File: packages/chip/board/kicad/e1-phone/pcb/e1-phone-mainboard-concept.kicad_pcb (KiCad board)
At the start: 10 copper layers, 64 x 132 mm, 87 parts

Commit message: chip(e1-phone): re-render exploded animation with corrected framing + lighting + EGL chunking
Visual self-review of the previous render exposed three defects that this commit closes:

- Camera was at radius 220 mm with 35deg yfov; phone is ~155 mm tall with parts that fly ~150 mm outward at peak explode, so the camera was effectively inside the explosion bubble. Bumped radius to 500 mm and narrowed yfov to 28deg; tilt to 15deg.
- Lights were camera-anchored, so the back of the orange shell went muddy during the 360deg orbit. Switched to world-anchored 3-point lighting.
- pyrender EGL leaked GPU memory and consistently died around frame ~150. Recreating OffscreenRenderer every 30 frames keeps the full 360-frame render stable.

Re-render output (all confirmed by reading 4 keyframes):
- e1-phone-exploded.mp4: 1920x1080, 30 fps, 12 s, h264/yuv420p, 897 KB
- e1-phone-exploded.glb: 98 nodes, 97 meshes, 3 clips (explode/reassemble/turntable), 183 KB
- e1-phone-exploded-frames/: 360 sequential frames + 24 keyframes at 0.5 s

Also restores the chip e1-phone artifacts (mechanical, board, supplier-pinouts, generator scripts) that an out-of-band git reset to origin/develop wiped between my previous commits ae3f83e9e7 / bd0a350198 and the current HEAD.

Co-Authored-By: Claude Opus 4.7 (1M context) <noreply@anthropic.com>
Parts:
- J_CAM0_CAM1: value rear_and_front_mipi_csi_cameras -> rear_and_front_mipi_csi_camera_fpc_connector_escape
- J_DISPLAY_TOUCH: value 5p5_in_fhd_mipi_display_touch -> 5p5_in_fhd_mipi_display_touch_fpc_connector_escape
- U_AUDIO_SPK_MIC: value speakers_microphones_audio_codec_haptics -> bottom_left_audio_codec_speaker_microphone_haptic_co
- moved U_AUDIO_SPK_MIC 19.6 mm to (14.0, 124.0)
- moved SW_POWER_VOL 14.0 mm to (24.0, 27.5)
- moved U_PMIC_CHARGER 13.7 mm to (24.5, 22.0)
- moved J_BATTERY 13.0 mm to (37.0, 28.0)
- moved J_DISPLAY_TOUCH 10.7 mm to (53.5, 7.00)
- moved U_CELL 7.52 mm to (10.0, 10.0)
- moved J_CAM0_CAM1 3.50 mm to (53.5, 18.5)
- moved U_WIFI_BT 2.50 mm to (10.0, 23.0)
- moved J_USB_C 2.00 mm to (34.0, 129.0)
- moved U_SOC_LPDDR_UFS 2.00 mm to (30.5, 10.0)
- moved RN_PMIC_CTL 1.20 mm to (38.0, 27.8)
- moved C_AON 1.00 mm to (18.0, 27.8)
- moved J_TOP_BOTTOM_FLEX_TOP 1.00 mm to (54.0, 27.5)
- moved RC_1 1.00 mm to (3.00, 27.8)
- moved RC_2 1.00 mm to (8.00, 27.8)
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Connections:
- J_TOP_BOTTOM_FLEX_BOTTOM pad 1: USB_DP -> GND
- J_TOP_BOTTOM_FLEX_BOTTOM pad 10: VDD_AUDIO_3V3 -> VBUS
- J_TOP_BOTTOM_FLEX_BOTTOM pad 11: VDD_AMP_3V3 -> GND
- J_TOP_BOTTOM_FLEX_BOTTOM pad 12: I2S_BCLK -> SYS
- J_TOP_BOTTOM_FLEX_BOTTOM pad 13: I2S_LRCLK -> GND
- J_TOP_BOTTOM_FLEX_BOTTOM pad 14: I2S_DOUT -> SYS
- J_TOP_BOTTOM_FLEX_BOTTOM pad 15: I2S_DIN -> AON_1V8
- J_TOP_BOTTOM_FLEX_BOTTOM pad 16: PDM_CLK -> GND
- J_TOP_BOTTOM_FLEX_BOTTOM pad 17: PDM_DAT -> IO_1V8
- J_TOP_BOTTOM_FLEX_BOTTOM pad 18: AUDIO_I2C_SCL -> GND
- J_TOP_BOTTOM_FLEX_BOTTOM pad 19: AUDIO_I2C_SDA -> VDD_AUDIO_3V3
- J_TOP_BOTTOM_FLEX_BOTTOM pad 2: USB_DN -> USB_DP
- J_TOP_BOTTOM_FLEX_BOTTOM pad 20: CODEC_INT -> VDD_AMP_3V3
- J_TOP_BOTTOM_FLEX_BOTTOM pad 21: AMP_INT -> GND
- J_TOP_BOTTOM_FLEX_BOTTOM pad 22: HAPTIC_OUT -> VBAT
- J_TOP_BOTTOM_FLEX_BOTTOM pad 23: VBAT -> GND
- J_TOP_BOTTOM_FLEX_BOTTOM pad 26: GND -> I2S_BCLK
- J_TOP_BOTTOM_FLEX_BOTTOM pad 28: GND -> I2S_LRCLK
- J_TOP_BOTTOM_FLEX_BOTTOM pad 29: GND -> I2S_DOUT
- J_TOP_BOTTOM_FLEX_BOTTOM pad 3: USB_CC1 -> USB_DN
- J_TOP_BOTTOM_FLEX_BOTTOM pad 30: GND -> I2S_DIN
- J_TOP_BOTTOM_FLEX_BOTTOM pad 32: GND -> PDM_CLK
- J_TOP_BOTTOM_FLEX_BOTTOM pad 34: GND -> PDM_DAT
- J_TOP_BOTTOM_FLEX_BOTTOM pad 35: GND -> AUDIO_I2C_SCL
- J_TOP_BOTTOM_FLEX_BOTTOM pad 36: GND -> AUDIO_I2C_SDA
- J_TOP_BOTTOM_FLEX_BOTTOM pad 37: GND -> CODEC_INT
- J_TOP_BOTTOM_FLEX_BOTTOM pad 38: GND -> AMP_INT
- J_TOP_BOTTOM_FLEX_BOTTOM pad 39: GND -> HAPTIC_OUT
- J_TOP_BOTTOM_FLEX_BOTTOM pad 4: USB_CC2 -> GND
- J_TOP_BOTTOM_FLEX_BOTTOM pad 41: GND -> (no net)
- J_TOP_BOTTOM_FLEX_BOTTOM pad 42: GND -> (no net)
- J_TOP_BOTTOM_FLEX_BOTTOM pad 43: GND -> (no net)
- J_TOP_BOTTOM_FLEX_BOTTOM pad 44: GND -> (no net)
- J_TOP_BOTTOM_FLEX_BOTTOM pad 45: GND -> (no net)
- J_TOP_BOTTOM_FLEX_BOTTOM pad 46: GND -> (no net)
- J_TOP_BOTTOM_FLEX_BOTTOM pad 5: VBUS -> SHIELD_GND
- J_TOP_BOTTOM_FLEX_BOTTOM pad 6: SHIELD_GND -> USB_CC1
- J_TOP_BOTTOM_FLEX_BOTTOM pad 7: SYS -> USB_CC2
- J_TOP_BOTTOM_FLEX_BOTTOM pad 8: AON_1V8 -> VBUS
- J_TOP_BOTTOM_FLEX_BOTTOM pad 9: IO_1V8 -> GND
- J_TOP_BOTTOM_FLEX_TOP pad 1: USB_DP -> GND
- J_TOP_BOTTOM_FLEX_TOP pad 10: VDD_AUDIO_3V3 -> VBUS
- J_TOP_BOTTOM_FLEX_TOP pad 11: VDD_AMP_3V3 -> GND
- J_TOP_BOTTOM_FLEX_TOP pad 12: I2S_BCLK -> SYS
- J_TOP_BOTTOM_FLEX_TOP pad 13: I2S_LRCLK -> GND
- J_TOP_BOTTOM_FLEX_TOP pad 14: I2S_DOUT -> SYS
- J_TOP_BOTTOM_FLEX_TOP pad 15: I2S_DIN -> AON_1V8
- J_TOP_BOTTOM_FLEX_TOP pad 16: PDM_CLK -> GND
- J_TOP_BOTTOM_FLEX_TOP pad 17: PDM_DAT -> IO_1V8
- J_TOP_BOTTOM_FLEX_TOP pad 18: AUDIO_I2C_SCL -> GND
- J_TOP_BOTTOM_FLEX_TOP pad 19: AUDIO_I2C_SDA -> VDD_AUDIO_3V3
- J_TOP_BOTTOM_FLEX_TOP pad 2: USB_DN -> USB_DP
- J_TOP_BOTTOM_FLEX_TOP pad 20: CODEC_INT -> VDD_AMP_3V3
- J_TOP_BOTTOM_FLEX_TOP pad 21: AMP_INT -> GND
- J_TOP_BOTTOM_FLEX_TOP pad 22: HAPTIC_OUT -> VBAT
- J_TOP_BOTTOM_FLEX_TOP pad 23: VBAT -> GND
- J_TOP_BOTTOM_FLEX_TOP pad 26: GND -> I2S_BCLK
- J_TOP_BOTTOM_FLEX_TOP pad 28: GND -> I2S_LRCLK
- J_TOP_BOTTOM_FLEX_TOP pad 29: GND -> I2S_DOUT
- J_TOP_BOTTOM_FLEX_TOP pad 3: USB_CC1 -> USB_DN
- J_TOP_BOTTOM_FLEX_TOP pad 30: GND -> I2S_DIN
- J_TOP_BOTTOM_FLEX_TOP pad 32: GND -> PDM_CLK
- J_TOP_BOTTOM_FLEX_TOP pad 34: GND -> PDM_DAT
- J_TOP_BOTTOM_FLEX_TOP pad 35: GND -> AUDIO_I2C_SCL
- J_TOP_BOTTOM_FLEX_TOP pad 36: GND -> AUDIO_I2C_SDA
- J_TOP_BOTTOM_FLEX_TOP pad 37: GND -> CODEC_INT
- J_TOP_BOTTOM_FLEX_TOP pad 38: GND -> AMP_INT
- J_TOP_BOTTOM_FLEX_TOP pad 39: GND -> HAPTIC_OUT
- J_TOP_BOTTOM_FLEX_TOP pad 4: USB_CC2 -> GND
- J_TOP_BOTTOM_FLEX_TOP pad 41: GND -> (no net)
- J_TOP_BOTTOM_FLEX_TOP pad 42: GND -> (no net)
- J_TOP_BOTTOM_FLEX_TOP pad 43: GND -> (no net)
- J_TOP_BOTTOM_FLEX_TOP pad 44: GND -> (no net)
- J_TOP_BOTTOM_FLEX_TOP pad 45: GND -> (no net)
- J_TOP_BOTTOM_FLEX_TOP pad 46: GND -> (no net)
- J_TOP_BOTTOM_FLEX_TOP pad 5: VBUS -> SHIELD_GND
- J_TOP_BOTTOM_FLEX_TOP pad 6: SHIELD_GND -> USB_CC1
- J_TOP_BOTTOM_FLEX_TOP pad 7: SYS -> USB_CC2
- J_TOP_BOTTOM_FLEX_TOP pad 8: AON_1V8 -> VBUS
- J_TOP_BOTTOM_FLEX_TOP pad 9: IO_1V8 -> GND
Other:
- net class E1Phone_AUDIO_ANALOG_HAPTIC added: clearance 0.160, trace_width 0.160, via_dia 0.300, via_drill 0.150
- net class E1Phone_DEBUG_BOOT added: clearance 0.100, trace_width 0.100, via_dia 0.250, via_drill 0.100
- net class E1Phone_DISPLAY_CAMERA_CONTROL added: clearance 0.100, trace_width 0.100, via_dia 0.250, via_drill 0.100
- net class E1Phone_POWER_SENSE_CONTROL added: clearance 0.100, trace_width 0.100, via_dia 0.250, via_drill 0.100
- net class E1Phone_USB_CC_PD_CONTROL added: clearance 0.100, trace_width 0.100, via_dia 0.250, via_drill 0.100
- net class E1Phone_WIRELESS_CONTROL_BT_UART added: clearance 0.100, trace_width 0.100, via_dia 0.250, via_drill 0.100

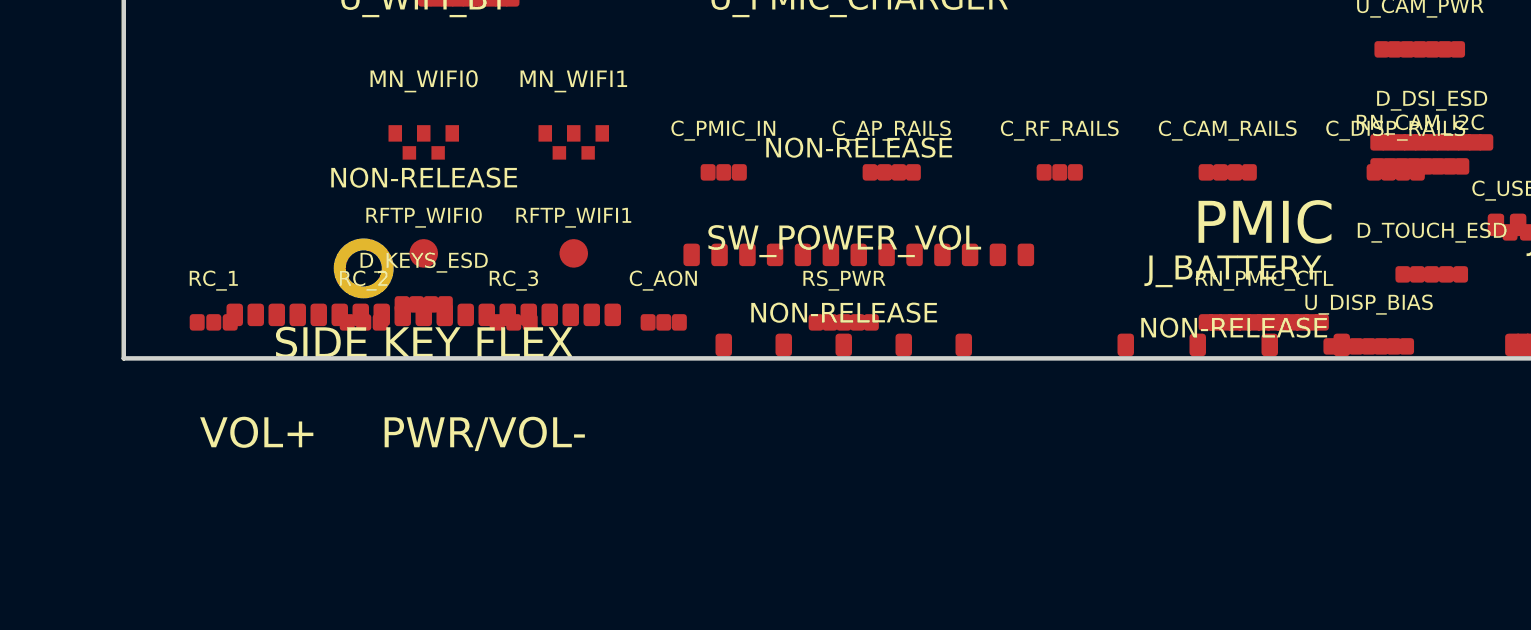
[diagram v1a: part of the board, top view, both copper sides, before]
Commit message: chore: snapshot in-flight working tree (chip/robot/android/os/riscv64/cloud)
WIP snapshot to avoid losing accumulated work across the chip board design,
robot RL + assets, android packaging, riscv64 port, and OS live-build dirs.
Generated artifacts and embedded vendor repos are excluded via .gitignore.

Co-Authored-By: Claude Opus 4.7 (1M context) <noreply@anthropic.com>
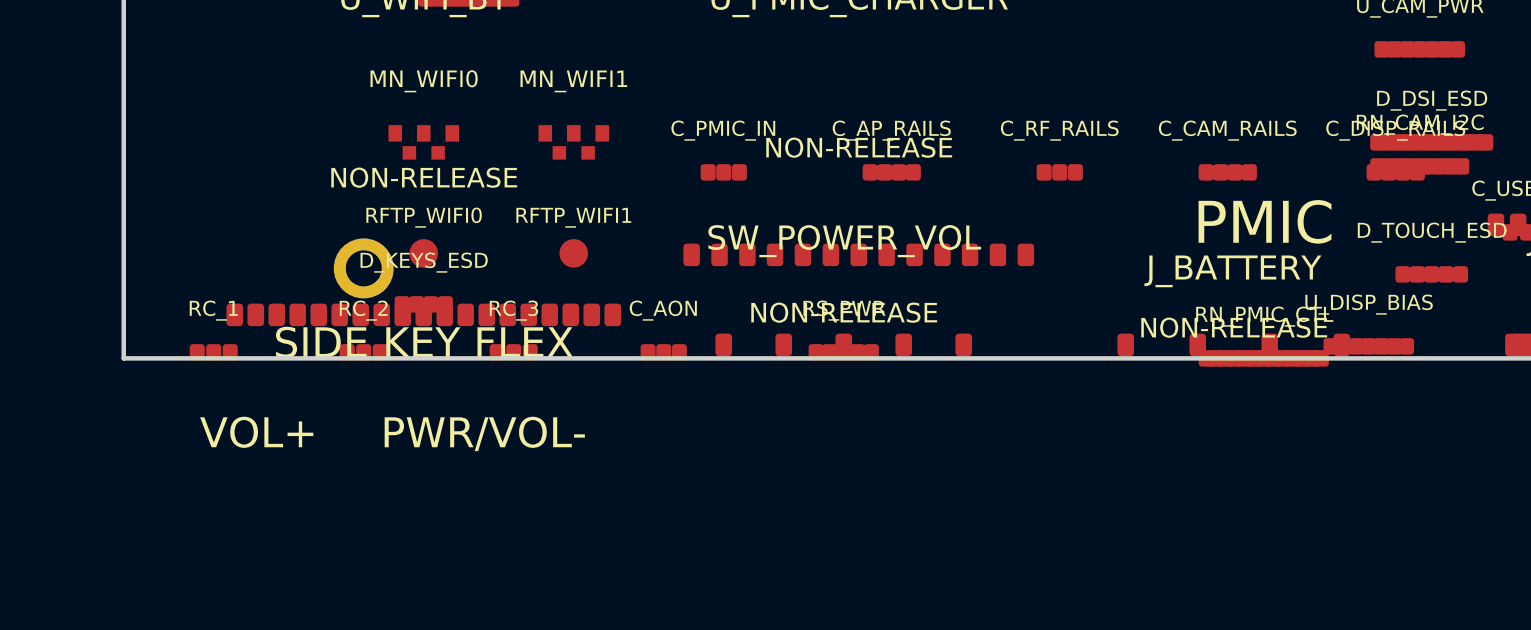
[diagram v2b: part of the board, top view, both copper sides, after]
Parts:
- moved RN_PMIC_CTL 1.20 mm to (38.0, 29.0)
- moved C_AON 1.00 mm to (18.0, 28.8)
- moved RC_1 1.00 mm to (3.00, 28.8)
- moved RC_2 1.00 mm to (8.00, 28.8)
- moved RC_3 1.00 mm to (13.0, 28.8)
- moved RS_PWR 1.00 mm to (24.0, 28.8)
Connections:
- J_TOP_BOTTOM_FLEX_BOTTOM pad 1: GND -> USB_DP
- J_TOP_BOTTOM_FLEX_BOTTOM pad 10: VBUS -> VDD_AUDIO_3V3
- J_TOP_BOTTOM_FLEX_BOTTOM pad 11: GND -> VDD_AMP_3V3
- J_TOP_BOTTOM_FLEX_BOTTOM pad 12: SYS -> I2S_BCLK
- J_TOP_BOTTOM_FLEX_BOTTOM pad 13: GND -> I2S_LRCLK
- J_TOP_BOTTOM_FLEX_BOTTOM pad 14: SYS -> I2S_DOUT
- J_TOP_BOTTOM_FLEX_BOTTOM pad 15: AON_1V8 -> I2S_DIN
- J_TOP_BOTTOM_FLEX_BOTTOM pad 16: GND -> PDM_CLK
- J_TOP_BOTTOM_FLEX_BOTTOM pad 17: IO_1V8 -> PDM_DAT
- J_TOP_BOTTOM_FLEX_BOTTOM pad 18: GND -> AUDIO_I2C_SCL
- J_TOP_BOTTOM_FLEX_BOTTOM pad 19: VDD_AUDIO_3V3 -> AUDIO_I2C_SDA
- J_TOP_BOTTOM_FLEX_BOTTOM pad 2: USB_DP -> USB_DN
- J_TOP_BOTTOM_FLEX_BOTTOM pad 20: VDD_AMP_3V3 -> CODEC_INT
- J_TOP_BOTTOM_FLEX_BOTTOM pad 21: GND -> AMP_INT
- J_TOP_BOTTOM_FLEX_BOTTOM pad 22: VBAT -> HAPTIC_OUT
- J_TOP_BOTTOM_FLEX_BOTTOM pad 23: GND -> VBAT
- J_TOP_BOTTOM_FLEX_BOTTOM pad 26: I2S_BCLK -> GND
- J_TOP_BOTTOM_FLEX_BOTTOM pad 28: I2S_LRCLK -> GND
- J_TOP_BOTTOM_FLEX_BOTTOM pad 29: I2S_DOUT -> GND
- J_TOP_BOTTOM_FLEX_BOTTOM pad 3: USB_DN -> USB_CC1
- J_TOP_BOTTOM_FLEX_BOTTOM pad 30: I2S_DIN -> GND
- J_TOP_BOTTOM_FLEX_BOTTOM pad 32: PDM_CLK -> GND
- J_TOP_BOTTOM_FLEX_BOTTOM pad 34: PDM_DAT -> GND
- J_TOP_BOTTOM_FLEX_BOTTOM pad 35: AUDIO_I2C_SCL -> GND
- J_TOP_BOTTOM_FLEX_BOTTOM pad 36: AUDIO_I2C_SDA -> GND
- J_TOP_BOTTOM_FLEX_BOTTOM pad 37: CODEC_INT -> GND
- J_TOP_BOTTOM_FLEX_BOTTOM pad 38: AMP_INT -> GND
- J_TOP_BOTTOM_FLEX_BOTTOM pad 39: HAPTIC_OUT -> GND
- J_TOP_BOTTOM_FLEX_BOTTOM pad 4: GND -> USB_CC2
- J_TOP_BOTTOM_FLEX_BOTTOM pad 41: (no net) -> GND
- J_TOP_BOTTOM_FLEX_BOTTOM pad 42: (no net) -> GND
- J_TOP_BOTTOM_FLEX_BOTTOM pad 43: (no net) -> GND
- J_TOP_BOTTOM_FLEX_BOTTOM pad 44: (no net) -> GND
- J_TOP_BOTTOM_FLEX_BOTTOM pad 45: (no net) -> GND
- J_TOP_BOTTOM_FLEX_BOTTOM pad 46: (no net) -> GND
- J_TOP_BOTTOM_FLEX_BOTTOM pad 5: SHIELD_GND -> VBUS
- J_TOP_BOTTOM_FLEX_BOTTOM pad 6: USB_CC1 -> SHIELD_GND
- J_TOP_BOTTOM_FLEX_BOTTOM pad 7: USB_CC2 -> SYS
- J_TOP_BOTTOM_FLEX_BOTTOM pad 8: VBUS -> AON_1V8
- J_TOP_BOTTOM_FLEX_BOTTOM pad 9: GND -> IO_1V8
- J_TOP_BOTTOM_FLEX_TOP pad 1: GND -> USB_DP
- J_TOP_BOTTOM_FLEX_TOP pad 10: VBUS -> VDD_AUDIO_3V3
- J_TOP_BOTTOM_FLEX_TOP pad 11: GND -> VDD_AMP_3V3
- J_TOP_BOTTOM_FLEX_TOP pad 12: SYS -> I2S_BCLK
- J_TOP_BOTTOM_FLEX_TOP pad 13: GND -> I2S_LRCLK
- J_TOP_BOTTOM_FLEX_TOP pad 14: SYS -> I2S_DOUT
- J_TOP_BOTTOM_FLEX_TOP pad 15: AON_1V8 -> I2S_DIN
- J_TOP_BOTTOM_FLEX_TOP pad 16: GND -> PDM_CLK
- J_TOP_BOTTOM_FLEX_TOP pad 17: IO_1V8 -> PDM_DAT
- J_TOP_BOTTOM_FLEX_TOP pad 18: GND -> AUDIO_I2C_SCL
- J_TOP_BOTTOM_FLEX_TOP pad 19: VDD_AUDIO_3V3 -> AUDIO_I2C_SDA
- J_TOP_BOTTOM_FLEX_TOP pad 2: USB_DP -> USB_DN
- J_TOP_BOTTOM_FLEX_TOP pad 20: VDD_AMP_3V3 -> CODEC_INT
- J_TOP_BOTTOM_FLEX_TOP pad 21: GND -> AMP_INT
- J_TOP_BOTTOM_FLEX_TOP pad 22: VBAT -> HAPTIC_OUT
- J_TOP_BOTTOM_FLEX_TOP pad 23: GND -> VBAT
- J_TOP_BOTTOM_FLEX_TOP pad 26: I2S_BCLK -> GND
- J_TOP_BOTTOM_FLEX_TOP pad 28: I2S_LRCLK -> GND
- J_TOP_BOTTOM_FLEX_TOP pad 29: I2S_DOUT -> GND
- J_TOP_BOTTOM_FLEX_TOP pad 3: USB_DN -> USB_CC1
- J_TOP_BOTTOM_FLEX_TOP pad 30: I2S_DIN -> GND
- J_TOP_BOTTOM_FLEX_TOP pad 32: PDM_CLK -> GND
- J_TOP_BOTTOM_FLEX_TOP pad 34: PDM_DAT -> GND
- J_TOP_BOTTOM_FLEX_TOP pad 35: AUDIO_I2C_SCL -> GND
- J_TOP_BOTTOM_FLEX_TOP pad 36: AUDIO_I2C_SDA -> GND
- J_TOP_BOTTOM_FLEX_TOP pad 37: CODEC_INT -> GND
- J_TOP_BOTTOM_FLEX_TOP pad 38: AMP_INT -> GND
- J_TOP_BOTTOM_FLEX_TOP pad 39: HAPTIC_OUT -> GND
- J_TOP_BOTTOM_FLEX_TOP pad 4: GND -> USB_CC2
- J_TOP_BOTTOM_FLEX_TOP pad 41: (no net) -> GND
- J_TOP_BOTTOM_FLEX_TOP pad 42: (no net) -> GND
- J_TOP_BOTTOM_FLEX_TOP pad 43: (no net) -> GND
- J_TOP_BOTTOM_FLEX_TOP pad 44: (no net) -> GND
- J_TOP_BOTTOM_FLEX_TOP pad 45: (no net) -> GND
- J_TOP_BOTTOM_FLEX_TOP pad 46: (no net) -> GND
- J_TOP_BOTTOM_FLEX_TOP pad 5: SHIELD_GND -> VBUS
- J_TOP_BOTTOM_FLEX_TOP pad 6: USB_CC1 -> SHIELD_GND
- J_TOP_BOTTOM_FLEX_TOP pad 7: USB_CC2 -> SYS
- J_TOP_BOTTOM_FLEX_TOP pad 8: VBUS -> AON_1V8
- J_TOP_BOTTOM_FLEX_TOP pad 9: GND -> IO_1V8
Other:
- net class E1Phone_AUDIO_ANALOG_HAPTIC removed
- net class E1Phone_DEBUG_BOOT removed
- net class E1Phone_DISPLAY_CAMERA_CONTROL removed
- net class E1Phone_POWER_SENSE_CONTROL removed
- net class E1Phone_USB_CC_PD_CONTROL removed
- net class E1Phone_WIRELESS_CONTROL_BT_UART removed
